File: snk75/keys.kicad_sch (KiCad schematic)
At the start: 48 parts

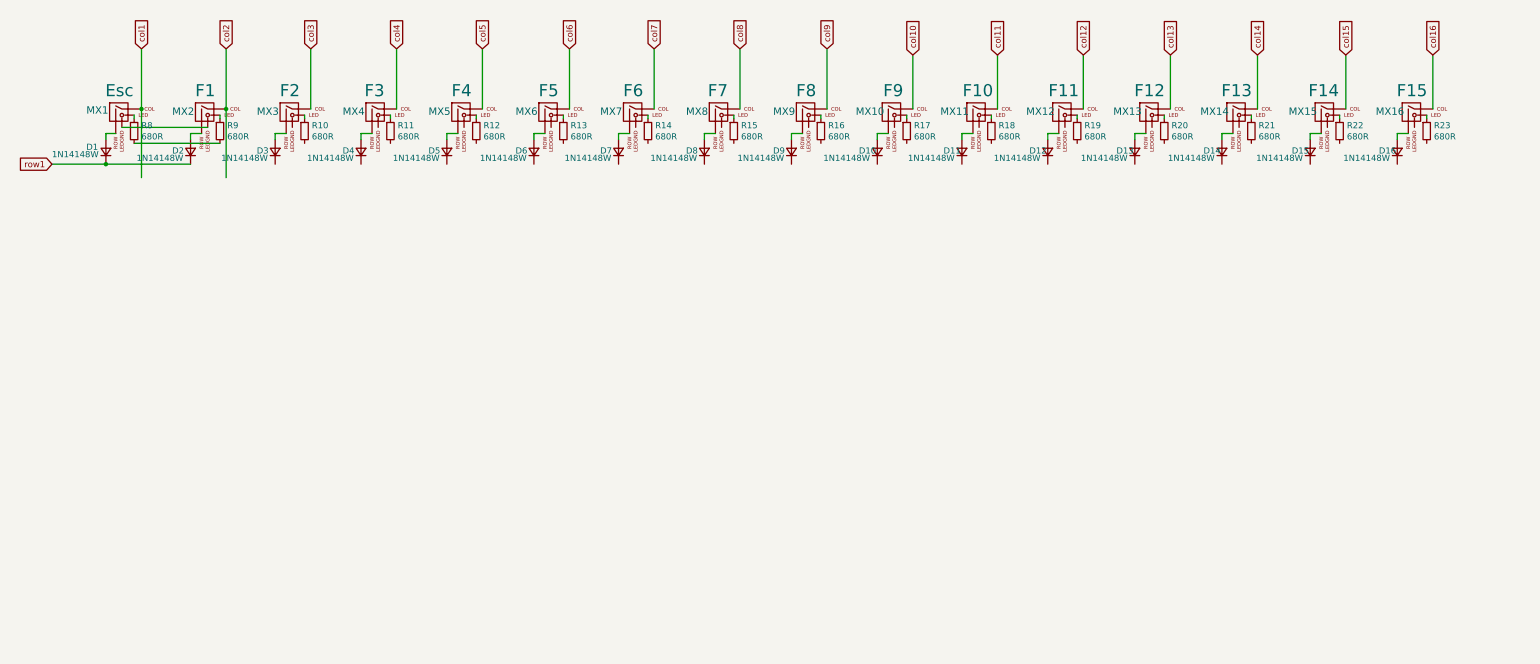
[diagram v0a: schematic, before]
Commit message: Add keys row 2
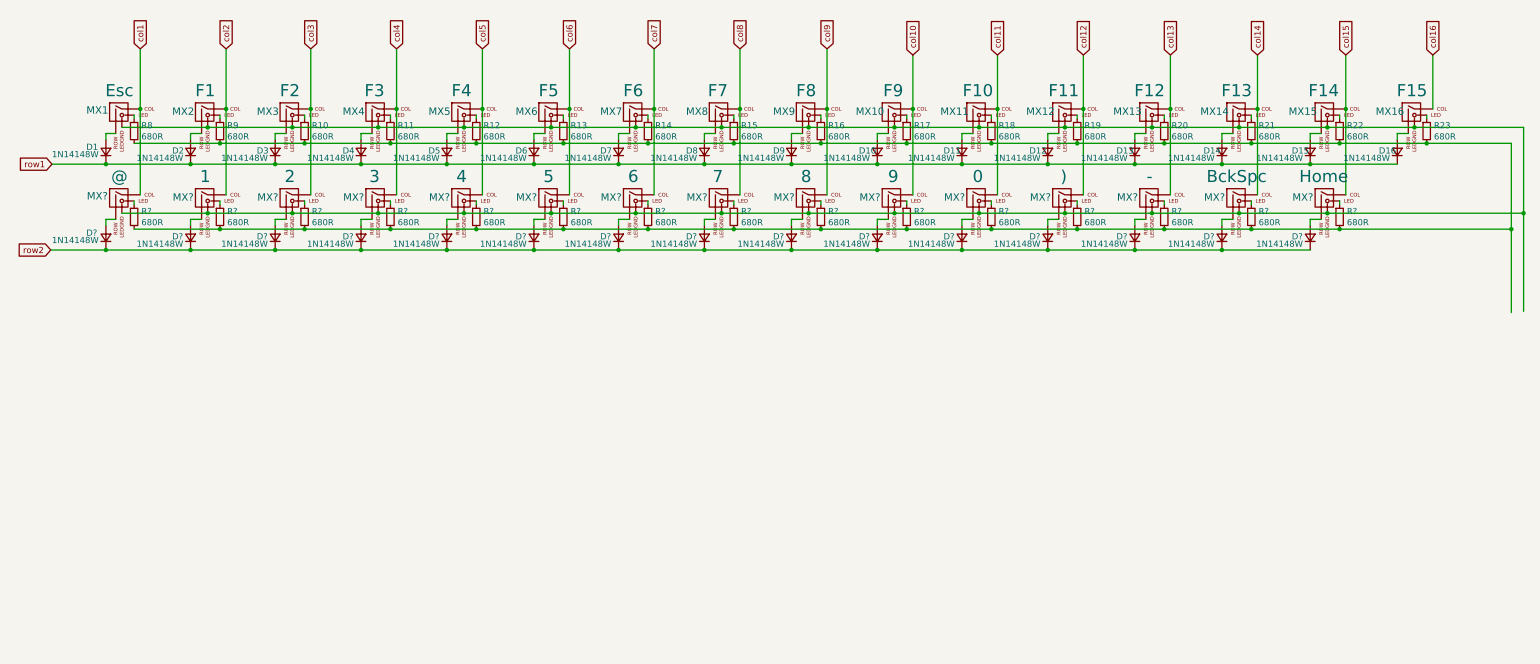
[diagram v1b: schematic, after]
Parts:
- added D? (x15): 1N14148W, Diode_SMD:D_SOD-123, symbol Device:D_Small
- added MX?: 5, MX_Only:MXOnly-1U, symbol MX_Alps_Hybrid:MX-LED
- added MX?: 1, MX_Only:MXOnly-1U, symbol MX_Alps_Hybrid:MX-LED
- added MX?: -, MX_Only:MXOnly-1U, symbol MX_Alps_Hybrid:MX-LED
- added MX?: ), MX_Only:MXOnly-1U, symbol MX_Alps_Hybrid:MX-LED
- added MX?: BckSpc, MX_Only:MXOnly-1U, symbol MX_Alps_Hybrid:MX-LED
- added MX?: @, MX_Only:MXOnly-1U, symbol MX_Alps_Hybrid:MX-LED
- added MX?: 7, MX_Only:MXOnly-1U, symbol MX_Alps_Hybrid:MX-LED
- added MX?: 9, MX_Only:MXOnly-1U, symbol MX_Alps_Hybrid:MX-LED
- added MX?: Home, MX_Only:MXOnly-1U, symbol MX_Alps_Hybrid:MX-LED
- added MX?: 0, MX_Only:MXOnly-1U, symbol MX_Alps_Hybrid:MX-LED
- added MX?: 6, MX_Only:MXOnly-1U, symbol MX_Alps_Hybrid:MX-LED
- added MX?: 8, MX_Only:MXOnly-1U, symbol MX_Alps_Hybrid:MX-LED
- added MX?: 3, MX_Only:MXOnly-1U, symbol MX_Alps_Hybrid:MX-LED
- added MX?: 2, MX_Only:MXOnly-1U, symbol MX_Alps_Hybrid:MX-LED
- added MX?: 4, MX_Only:MXOnly-1U, symbol MX_Alps_Hybrid:MX-LED
- added R? (x15): 680R, Resistor_SMD:R_1206_3216Metric_Pad1.30x1.75mm_HandSolder, symbol Device:R_Small
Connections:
- net col1: now also MX?.1 (COL)
- net col10: now also MX?.1 (COL)
- net col11: now also MX?.1 (COL)
- net col12: now also MX?.1 (COL)
- net col13: now also MX?.1 (COL)
- net col14: now also MX?.1 (COL)
- net col15: now also MX?.1 (COL)
- net col2: now also MX?.1 (COL)
- net col3: now also MX?.1 (COL)
- net col4: now also MX?.1 (COL)
- net col5: now also MX?.1 (COL)
- net col6: now also MX?.1 (COL)
- net col7: now also MX?.1 (COL)
- net col8: now also MX?.1 (COL)
- net col9: now also MX?.1 (COL)
- net row1: now also D10.1 (K), D11.1 (K), D12.1 (K), D13.1 (K), D14.1 (K), D15.1 (K), D16.1 (K), D3.1 (K), D4.1 (K), D5.1 (K), D6.1 (K), D7.1 (K), D8.1 (K), D9.1 (K)
- net at MX12.4 (LEDGND): now also MX1.4 (LEDGND), MX10.4 (LEDGND), MX11.4 (LEDGND), MX13.4 (LEDGND), MX14.4 (LEDGND), MX15.4 (LEDGND), MX16.4 (LEDGND), MX2.4 (LEDGND), MX3.4 (LEDGND), MX4.4 (LEDGND), MX5.4 (LEDGND), MX6.4 (LEDGND), MX7.4 (LEDGND), MX8.4 (LEDGND), MX9.4 (LEDGND), MX?.4 (LEDGND), MX?.4 (LEDGND), MX?.4 (LEDGND), MX?.4 (LEDGND), MX?.4 (LEDGND), MX?.4 (LEDGND), MX?.4 (LEDGND), MX?.4 (LEDGND), MX?.4 (LEDGND), MX?.4 (LEDGND), MX?.4 (LEDGND), MX?.4 (LEDGND), MX?.4 (LEDGND), MX?.4 (LEDGND), MX?.4 (LEDGND)
- net at R17.2: now also R10.2, R11.2, R12.2, R13.2, R14.2, R15.2, R16.2, R18.2, R19.2, R20.2, R21.2, R22.2, R23.2, R8.2, R9.2, R?.2, R?.2, R?.2, R?.2, R?.2, R?.2, R?.2, R?.2, R?.2, R?.2, R?.2, R?.2, R?.2, R?.2, R?.2
- new net: MX?.3 (LED), R?.1 (x15)
- new net: D?.2 (A), MX?.2 (ROW) (x15)
- new net row2: D?.1 (K), D?.1 (K), D?.1 (K), D?.1 (K), D?.1 (K), D?.1 (K), D?.1 (K), D?.1 (K), D?.1 (K), D?.1 (K), D?.1 (K), D?.1 (K), D?.1 (K), D?.1 (K), D?.1 (K)

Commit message: Added other keys
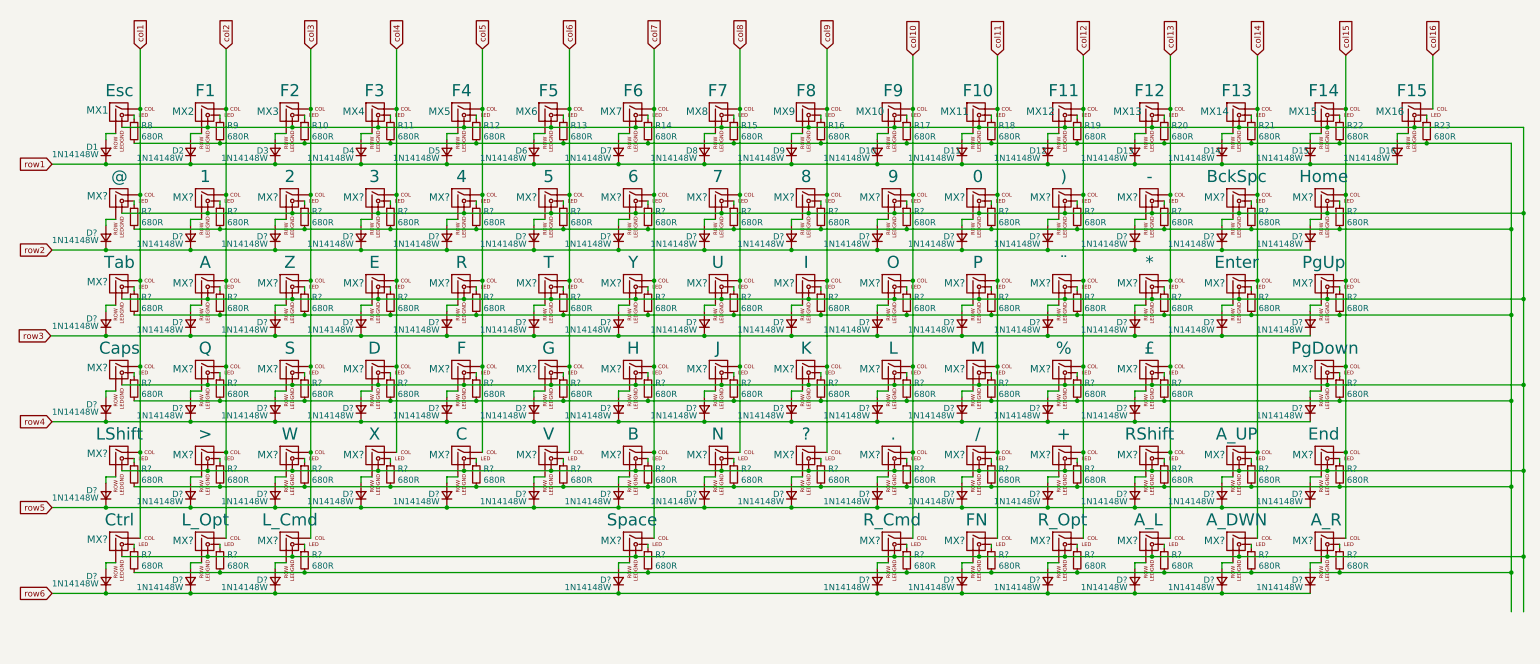
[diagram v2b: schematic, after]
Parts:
- added D? (x54): 1N14148W, Diode_SMD:D_SOD-123, symbol Device:D_Small
- added MX?: A_L, MX_Only:MXOnly-1U, symbol MX_Alps_Hybrid:MX-LED
- added MX?: LShift, MX_Only:MXOnly-1U, symbol MX_Alps_Hybrid:MX-LED
- added MX?: L_Opt, MX_Only:MXOnly-1U, symbol MX_Alps_Hybrid:MX-LED
- added MX?: K, MX_Only:MXOnly-1U, symbol MX_Alps_Hybrid:MX-LED
- added MX?: G, MX_Only:MXOnly-1U, symbol MX_Alps_Hybrid:MX-LED
- added MX?: End, MX_Only:MXOnly-1U, symbol MX_Alps_Hybrid:MX-LED
- added MX?: O, MX_Only:MXOnly-1U, symbol MX_Alps_Hybrid:MX-LED
- added MX?: N, MX_Only:MXOnly-1U, symbol MX_Alps_Hybrid:MX-LED
- added MX?: ¨, MX_Only:MXOnly-1U, symbol MX_Alps_Hybrid:MX-LED
- added MX?: B, MX_Only:MXOnly-1U, symbol MX_Alps_Hybrid:MX-LED
- added MX?: U, MX_Only:MXOnly-1U, symbol MX_Alps_Hybrid:MX-LED
- added MX?: Z, MX_Only:MXOnly-1U, symbol MX_Alps_Hybrid:MX-LED
- added MX?: PgDown, MX_Only:MXOnly-1U, symbol MX_Alps_Hybrid:MX-LED
- added MX?: /, MX_Only:MXOnly-1U, symbol MX_Alps_Hybrid:MX-LED
- added MX?: Caps, MX_Only:MXOnly-1U, symbol MX_Alps_Hybrid:MX-LED
- added MX?: %, MX_Only:MXOnly-1U, symbol MX_Alps_Hybrid:MX-LED
- added MX?: H, MX_Only:MXOnly-1U, symbol MX_Alps_Hybrid:MX-LED
- added MX?: Ctrl, MX_Only:MXOnly-1U, symbol MX_Alps_Hybrid:MX-LED
- added MX?: W, MX_Only:MXOnly-1U, symbol MX_Alps_Hybrid:MX-LED
- added MX?: D, MX_Only:MXOnly-1U, symbol MX_Alps_Hybrid:MX-LED
- added MX?: ?, MX_Only:MXOnly-1U, symbol MX_Alps_Hybrid:MX-LED
- added MX?: R_Cmd, MX_Only:MXOnly-1U, symbol MX_Alps_Hybrid:MX-LED
- added MX?: £, MX_Only:MXOnly-1U, symbol MX_Alps_Hybrid:MX-LED
- added MX?: X, MX_Only:MXOnly-1U, symbol MX_Alps_Hybrid:MX-LED
- added MX?: A, MX_Only:MXOnly-1U, symbol MX_Alps_Hybrid:MX-LED
- added MX?: PgUp, MX_Only:MXOnly-1U, symbol MX_Alps_Hybrid:MX-LED
- added MX?: *, MX_Only:MXOnly-1U, symbol MX_Alps_Hybrid:MX-LED
- added MX?: Y, MX_Only:MXOnly-1U, symbol MX_Alps_Hybrid:MX-LED
- added MX?: FN, MX_Only:MXOnly-1U, symbol MX_Alps_Hybrid:MX-LED
- added MX?: T, MX_Only:MXOnly-1U, symbol MX_Alps_Hybrid:MX-LED
- added MX?: J, MX_Only:MXOnly-1U, symbol MX_Alps_Hybrid:MX-LED
- added MX?: Enter, MX_Only:MXOnly-1U, symbol MX_Alps_Hybrid:MX-LED
- added MX?: P, MX_Only:MXOnly-1U, symbol MX_Alps_Hybrid:MX-LED
- added MX?: A_DWN, MX_Only:MXOnly-1U, symbol MX_Alps_Hybrid:MX-LED
- added MX?: R, MX_Only:MXOnly-1U, symbol MX_Alps_Hybrid:MX-LED
- added MX?: R_Opt, MX_Only:MXOnly-1U, symbol MX_Alps_Hybrid:MX-LED
- added MX?: S, MX_Only:MXOnly-1U, symbol MX_Alps_Hybrid:MX-LED
- added MX?: L_Cmd, MX_Only:MXOnly-1U, symbol MX_Alps_Hybrid:MX-LED
- added MX?: V, MX_Only:MXOnly-1U, symbol MX_Alps_Hybrid:MX-LED
- added MX?: L, MX_Only:MXOnly-1U, symbol MX_Alps_Hybrid:MX-LED
- added MX?: ., MX_Only:MXOnly-1U, symbol MX_Alps_Hybrid:MX-LED
- added MX?: F, MX_Only:MXOnly-1U, symbol MX_Alps_Hybrid:MX-LED
- added MX?: Space, MX_Only:MXOnly-1U, symbol MX_Alps_Hybrid:MX-LED
- added MX?: I, MX_Only:MXOnly-1U, symbol MX_Alps_Hybrid:MX-LED
- added MX?: Q, MX_Only:MXOnly-1U, symbol MX_Alps_Hybrid:MX-LED
- added MX?: M, MX_Only:MXOnly-1U, symbol MX_Alps_Hybrid:MX-LED
- added MX?: E, MX_Only:MXOnly-1U, symbol MX_Alps_Hybrid:MX-LED
- added MX?: +, MX_Only:MXOnly-1U, symbol MX_Alps_Hybrid:MX-LED
- added MX?: RShift, MX_Only:MXOnly-1U, symbol MX_Alps_Hybrid:MX-LED
- added MX?: A_UP, MX_Only:MXOnly-1U, symbol MX_Alps_Hybrid:MX-LED
- added MX?: C, MX_Only:MXOnly-1U, symbol MX_Alps_Hybrid:MX-LED
- added MX?: >, MX_Only:MXOnly-1U, symbol MX_Alps_Hybrid:MX-LED
- added MX?: A_R, MX_Only:MXOnly-1U, symbol MX_Alps_Hybrid:MX-LED
- added MX?: Tab, MX_Only:MXOnly-1U, symbol MX_Alps_Hybrid:MX-LED
- added R? (x54): 680R, Resistor_SMD:R_1206_3216Metric_Pad1.30x1.75mm_HandSolder, symbol Device:R_Small
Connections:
- net col1: now also MX?.1 (COL), MX?.1 (COL), MX?.1 (COL), MX?.1 (COL)
- net col10: now also MX?.1 (COL), MX?.1 (COL), MX?.1 (COL), MX?.1 (COL)
- net col11: now also MX?.1 (COL), MX?.1 (COL), MX?.1 (COL), MX?.1 (COL)
- net col12: now also MX?.1 (COL), MX?.1 (COL), MX?.1 (COL), MX?.1 (COL)
- net col13: now also MX?.1 (COL), MX?.1 (COL), MX?.1 (COL), MX?.1 (COL)
- net col14: now also MX?.1 (COL), MX?.1 (COL), MX?.1 (COL)
- net col15: now also MX?.1 (COL), MX?.1 (COL), MX?.1 (COL), MX?.1 (COL)
- net col2: now also MX?.1 (COL), MX?.1 (COL), MX?.1 (COL), MX?.1 (COL)
- net col3: now also MX?.1 (COL), MX?.1 (COL), MX?.1 (COL), MX?.1 (COL)
- net col4: now also MX?.1 (COL), MX?.1 (COL), MX?.1 (COL)
- net col5: now also MX?.1 (COL), MX?.1 (COL), MX?.1 (COL)
- net col6: now also MX?.1 (COL), MX?.1 (COL), MX?.1 (COL)
- net col7: now also MX?.1 (COL), MX?.1 (COL), MX?.1 (COL), MX?.1 (COL)
- net col8: now also MX?.1 (COL), MX?.1 (COL), MX?.1 (COL)
- net col9: now also MX?.1 (COL), MX?.1 (COL), MX?.1 (COL)
- net at R10.2, R11.2, R12.2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: now also R?.2, R?.2, R?.2, R?.2, R?.2, R?.2, R?.2, R?.2, R?.2, R?.2, R?.2, R?.2, R?.2, R?.2, R?.2, R?.2, R?.2, R?.2, R?.2, R?.2, R?.2, R?.2, R?.2, R?.2, R?.2, R?.2, R?.2, R?.2, R?.2, R?.2, R?.2, R?.2, R?.2, R?.2, R?.2, R?.2, R?.2, R?.2, R?.2, R?.2, R?.2, R?.2, R?.2, R?.2, R?.2, R?.2, R?.2, R?.2, R?.2, R?.2, R?.2, R?.2, R?.2, R?.2
- net at MX1.4 (LEDGND), MX10.4 (LEDGND), MX11.4 (LEDGND)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: now also MX?.4 (LEDGND), MX?.4 (LEDGND), MX?.4 (LEDGND), MX?.4 (LEDGND), MX?.4 (LEDGND), MX?.4 (LEDGND), MX?.4 (LEDGND), MX?.4 (LEDGND), MX?.4 (LEDGND), MX?.4 (LEDGND), MX?.4 (LEDGND), MX?.4 (LEDGND), MX?.4 (LEDGND), MX?.4 (LEDGND), MX?.4 (LEDGND), MX?.4 (LEDGND), MX?.4 (LEDGND), MX?.4 (LEDGND), MX?.4 (LEDGND), MX?.4 (LEDGND), MX?.4 (LEDGND), MX?.4 (LEDGND), MX?.4 (LEDGND), MX?.4 (LEDGND), MX?.4 (LEDGND), MX?.4 (LEDGND), MX?.4 (LEDGND), MX?.4 (LEDGND), MX?.4 (LEDGND), MX?.4 (LEDGND), MX?.4 (LEDGND), MX?.4 (LEDGND), MX?.4 (LEDGND), MX?.4 (LEDGND), MX?.4 (LEDGND), MX?.4 (LEDGND), MX?.4 (LEDGND), MX?.4 (LEDGND), MX?.4 (LEDGND), MX?.4 (LEDGND), MX?.4 (LEDGND), MX?.4 (LEDGND), MX?.4 (LEDGND), MX?.4 (LEDGND), MX?.4 (LEDGND), MX?.4 (LEDGND), MX?.4 (LEDGND), MX?.4 (LEDGND), MX?.4 (LEDGND), MX?.4 (LEDGND), MX?.4 (LEDGND), MX?.4 (LEDGND), MX?.4 (LEDGND), MX?.4 (LEDGND)
- new net: MX?.3 (LED), R?.1 (x54)
- new net: D?.2 (A), MX?.2 (ROW) (x54)
- new net row3: D?.1 (K), D?.1 (K), D?.1 (K), D?.1 (K), D?.1 (K), D?.1 (K), D?.1 (K), D?.1 (K), D?.1 (K), D?.1 (K), D?.1 (K), D?.1 (K), D?.1 (K), D?.1 (K), D?.1 (K)
- new net row4: D?.1 (K), D?.1 (K), D?.1 (K), D?.1 (K), D?.1 (K), D?.1 (K), D?.1 (K), D?.1 (K), D?.1 (K), D?.1 (K), D?.1 (K), D?.1 (K), D?.1 (K), D?.1 (K)
- new net row5: D?.1 (K), D?.1 (K), D?.1 (K), D?.1 (K), D?.1 (K), D?.1 (K), D?.1 (K), D?.1 (K), D?.1 (K), D?.1 (K), D?.1 (K), D?.1 (K), D?.1 (K), D?.1 (K), D?.1 (K)
- new net row6: D?.1 (K), D?.1 (K), D?.1 (K), D?.1 (K), D?.1 (K), D?.1 (K), D?.1 (K), D?.1 (K), D?.1 (K), D?.1 (K)

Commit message: Added u for not 1 unit keys
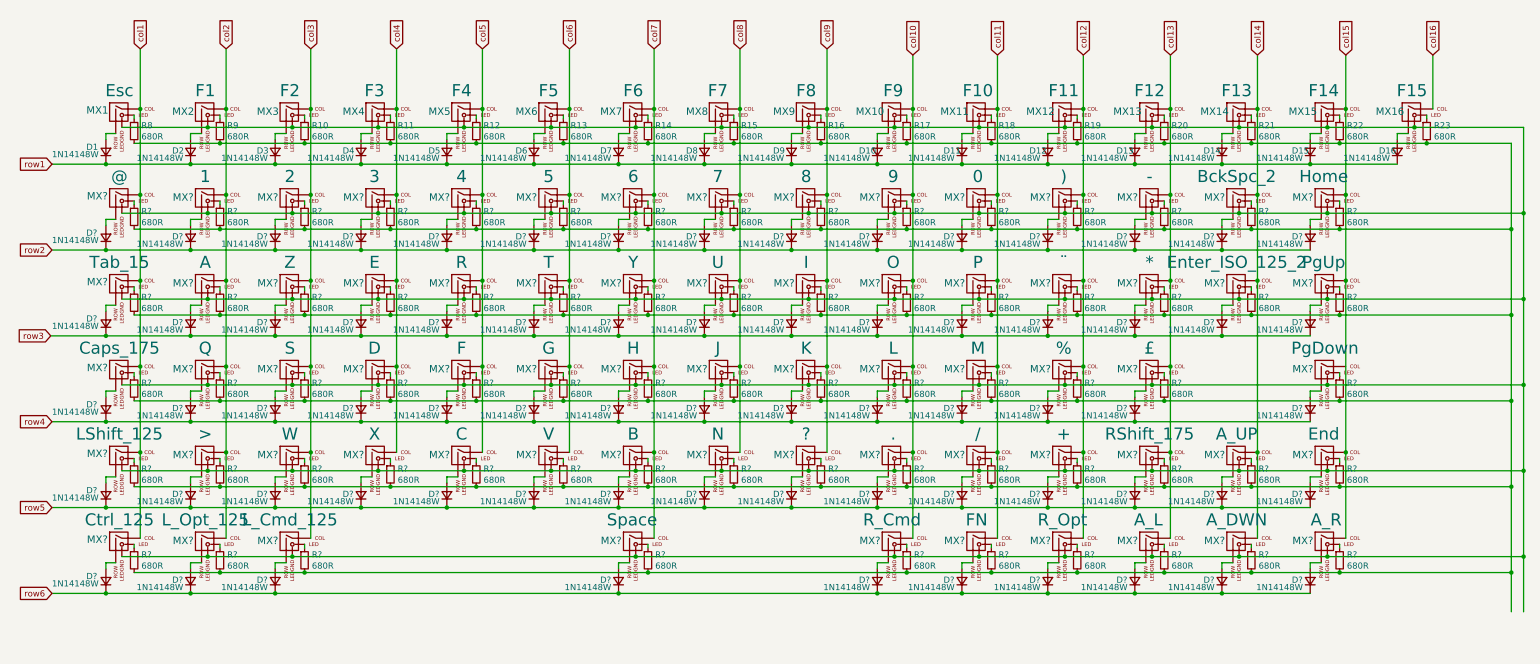
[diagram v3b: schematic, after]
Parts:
- MX?: value LShift -> LShift_125
- MX?: value L_Opt -> L_Opt_125
- MX?: value BckSpc -> BckSpc_2
- MX?: value Caps -> Caps_175
- MX?: value Ctrl -> Ctrl_125
- MX?: value Enter -> Enter_ISO_125_2
- MX?: value L_Cmd -> L_Cmd_125
- MX?: value RShift -> RShift_175
- MX?: value Tab -> Tab_15
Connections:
- net col15: no longer MX?.1 (COL)
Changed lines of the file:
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@@
   (junction (at 263.144 132.842) (diameter 0) (color 0 0 0 0)
   )
+  (junction (at 311.404 48.26) (diameter 0) (color 0 0 0 0)
+  )
   (junction (at 156.718 43.942) (diameter 0) (color 0 0 0 0)
   )
@@
   (junction (at 257.048 66.04) (diameter 0) (color 0 0 0 0)
   )
-  (junction (at 318.77 90.17) (diameter 0) (color 0 0 0 0)
-  )
   (junction (at 257.048 137.16) (diameter 0) (color 0 0 0 0)
   )
@@
   (junction (at 122.174 54.61) (diameter 0) (color 0 0 0 0)
   )
-  (junction (at 311.404 48.26) (diameter 0) (color 0 0 0 0)
-  )
   (junction (at 355.6 129.54) (diameter 0) (color 0 0 0 0)
   )
@@
     (stroke (width 0) (type default) (color 0 0 0 0))
   )
-  (wire (pts (xy 318.77 90.17) (xy 318.77 107.95))
+  (wire (pts (xy 318.77 72.39) (xy 318.77 107.95))
     (stroke (width 0) (type default) (color 0 0 0 0))
   )
@@
     (stroke (width 0) (type default) (color 0 0 0 0))
   )
-  (wire (pts (xy 311.404 48.26) (xy 329.438 48.26))
-    (stroke (width 0) (type default) (color 0 0 0 0))
-  )
   (wire (pts (xy 313.69 95.25) (xy 311.404 95.25))
     (stroke (width 0) (type default) (color 0 0 0 0))
@@
     (stroke (width 0) (type default) (color 0 0 0 0))
   )
-  (wire (pts (xy 300.482 72.39) (xy 300.482 107.95))
-    (stroke (width 0) (type default) (color 0 0 0 0))
-  )
   (wire (pts (xy 281.178 43.942) (xy 299.212 43.942))
     (stroke (width 0) (type default) (color 0 0 0 0))
@@
     (stroke (width 0) (type default) (color 0 0 0 0))
   )
+  (wire (pts (xy 300.482 72.39) (xy 300.482 107.95))
+    (stroke (width 0) (type default) (color 0 0 0 0))
+  )
   (wire (pts (xy 103.124 61.722) (xy 120.904 61.722))
     (stroke (width 0) (type default) (color 0 0 0 0))
@@
     (stroke (width 0) (type default) (color 0 0 0 0))
   )
-  (wire (pts (xy 318.77 72.39) (xy 318.77 90.17))
-    (stroke (width 0) (type default) (color 0 0 0 0))
-  )
   (wire (pts (xy 138.684 97.282) (xy 156.718 97.282))
     (stroke (width 0) (type default) (color 0 0 0 0))
@@
     (stroke (width 0) (type default) (color 0 0 0 0))
   )
+  (wire (pts (xy 311.404 48.26) (xy 329.438 48.26))
+    (stroke (width 0) (type default) (color 0 0 0 0))
+  )
   (wire (pts (xy 100.584 111.76) (xy 118.364 111.76))
     (stroke (width 0) (type default) (color 0 0 0 0))
@@
       (effects (font (size 1.524 1.524)))
     )
-    (property "Value" "LShift" (id 1) (at 64.77 104.14 0)
+    (property "Value" "LShift_125" (id 1) (at 64.77 104.14 0)
       (effects (font (size 2.5 2.5)))
     )
@@
       (effects (font (size 1.524 1.524)))
     )
-    (property "Value" "L_Opt" (id 1) (at 82.55 121.92 0)
+    (property "Value" "L_Opt_125" (id 1) (at 82.55 121.92 0)
       (effects (font (size 2.5 2.5)))
     )
@@
       (effects (font (size 1.524 1.524)))
     )
-    (property "Value" "BckSpc" (id 1) (at 296.164 50.8 0)
+    (property "Value" "BckSpc_2" (id 1) (at 296.164 50.8 0)
       (effects (font (size 2.5 2.5)))
     )
@@
       (effects (font (size 1.524 1.524)))
     )
-    (property "Value" "Caps" (id 1) (at 64.77 86.36 0)
+    (property "Value" "Caps_175" (id 1) (at 64.77 86.36 0)
       (effects (font (size 2.5 2.5)))
     )
@@
       (effects (font (size 1.524 1.524)))
     )
-    (property "Value" "Ctrl" (id 1) (at 64.77 121.92 0)
+    (property "Value" "Ctrl_125" (id 1) (at 64.77 121.92 0)
       (effects (font (size 2.5 2.5)))
     )
@@
       (effects (font (size 1.524 1.524)))
     )
-    (property "Value" "Enter" (id 1) (at 296.164 68.58 0)
+    (property "Value" "Enter_ISO_125_2" (id 1) (at 296.164 68.58 0)
       (effects (font (size 2.5 2.5)))
     )
@@
       (effects (font (size 1.524 1.524)))
     )
-    (property "Value" "L_Cmd" (id 1) (at 100.076 121.92 0)
+    (property "Value" "L_Cmd_125" (id 1) (at 100.076 121.92 0)
       (effects (font (size 2.5 2.5)))
     )
@@
       (effects (font (size 1.524 1.524)))
     )
-    (property "Value" "RShift" (id 1) (at 278.13 104.14 0)
+    (property "Value" "RShift_175" (id 1) (at 278.13 104.14 0)
       (effects (font (size 2.5 2.5)))
     )
@@
       (effects (font (size 1.524 1.524)))
     )
-    (property "Value" "Tab" (id 1) (at 64.77 68.58 0)
+    (property "Value" "Tab_15" (id 1) (at 64.77 68.58 0)
       (effects (font (size 2.5 2.5)))
     )

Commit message: Added u for not space
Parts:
- MX?: value Space -> Space_625
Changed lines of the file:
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@@
       (effects (font (size 1.524 1.524)))
     )
-    (property "Value" "Space" (id 1) (at 170.942 121.92 0)
+    (property "Value" "Space_625" (id 1) (at 170.942 121.92 0)
       (effects (font (size 2.5 2.5)))
     )
